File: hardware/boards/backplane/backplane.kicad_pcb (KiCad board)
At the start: 2 copper layers, 47 parts, among them J1 SPARE_I2C, J10 I2C_IN, J11 I2C_OUT, J12 LED_EXT_OUT, J14 DC_IN, J2 SLOT_4, J3 SLOT_1, J4 SLOT_2, J5 SLOT_5, J6 SLOT_6, J7 SLOT_3, J8 LED_EXT_IN, U1 TCA9548APWR, U2 USBLC6-2SC6, U3 USBLC6-2SC6, U4 USBLC6-2SC6, U5 USBLC6-2SC6, U6 USBLC6-2SC6, U7 USBLC6-2SC6

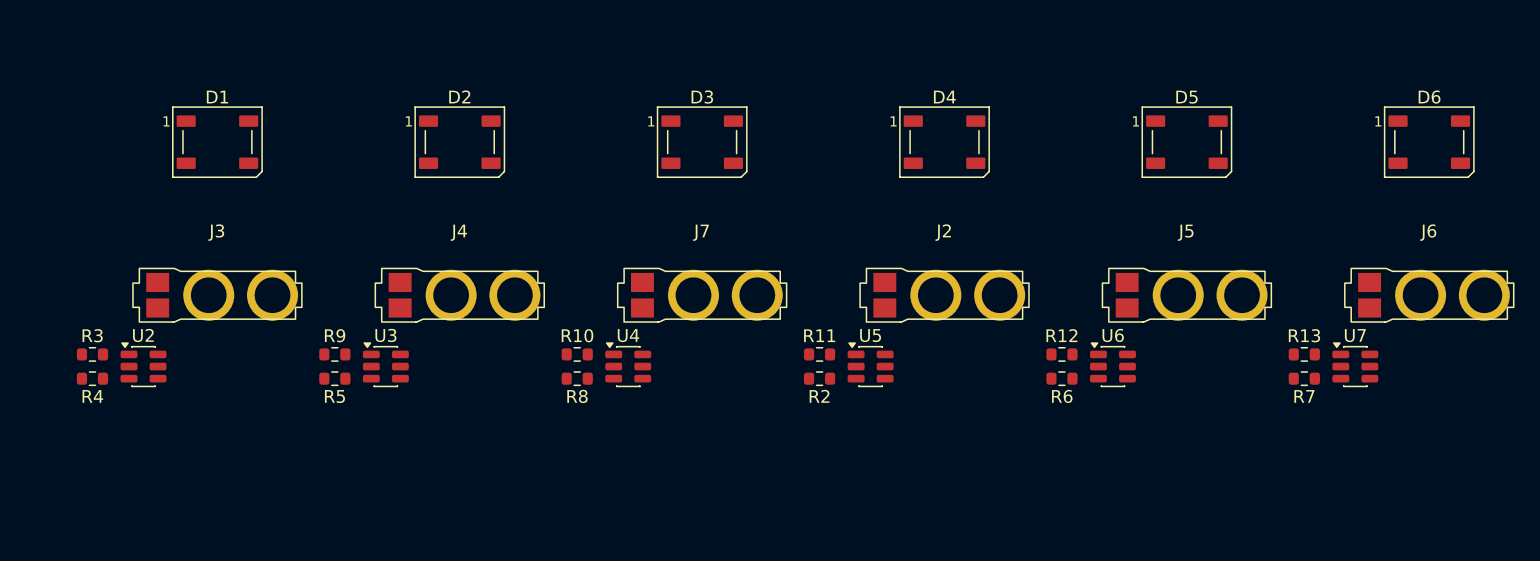
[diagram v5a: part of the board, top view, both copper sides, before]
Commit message: Reorient backplane slot component groups
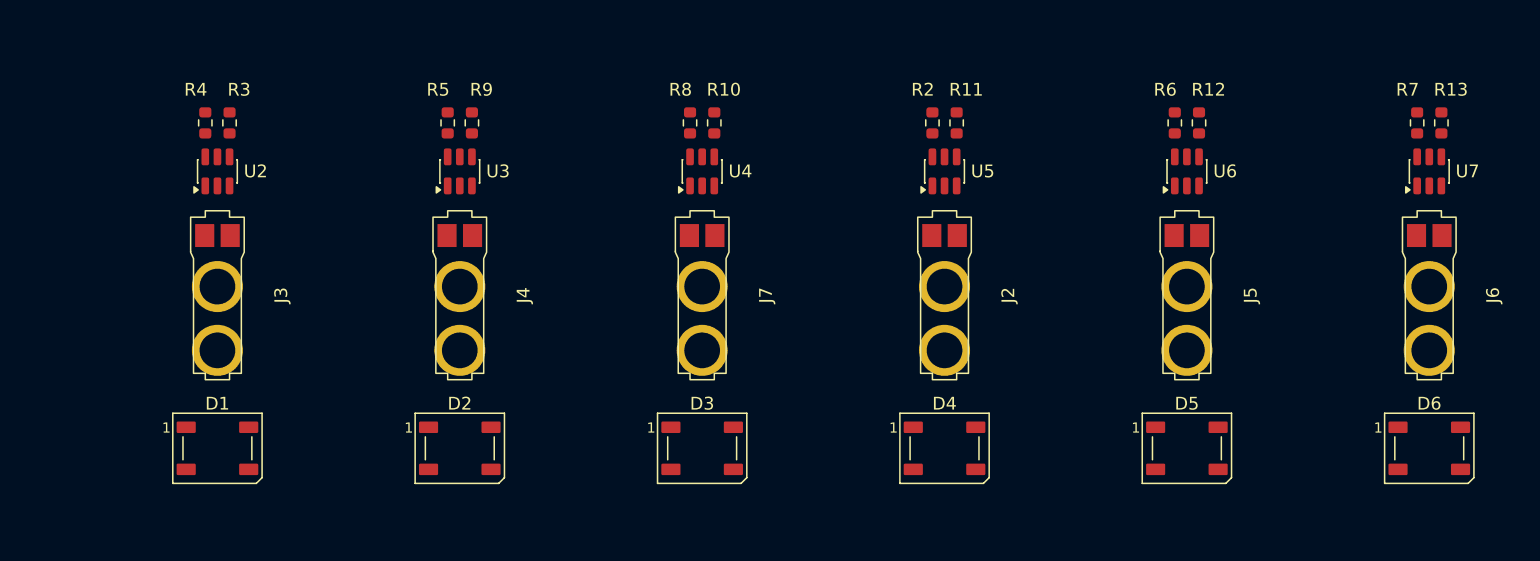
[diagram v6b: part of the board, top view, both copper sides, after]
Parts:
- moved D1 24.0 mm to (68.8, 76.9)
- moved D2 24.0 mm to (87.8, 76.9)
- moved D3 24.0 mm to (106.8, 76.9)
- moved D4 24.0 mm to (125.8, 76.9)
- moved D5 24.0 mm to (144.8, 76.9)
- moved D6 24.0 mm to (163.8, 76.9)
- moved R2 21.9 mm to (124.8, 51.4), turned to 90 degrees
- moved R4 21.9 mm to (67.8, 51.4), turned to 90 degrees
- moved R5 21.9 mm to (86.8, 51.4), turned to 90 degrees
- moved R6 21.9 mm to (143.8, 51.4), turned to 90 degrees
- moved R7 21.9 mm to (162.8, 51.4), turned to 90 degrees
- moved R8 21.9 mm to (105.8, 51.4), turned to 90 degrees
- moved R10 21.1 mm to (107.7, 51.4), turned to 90 degrees
- moved R11 21.1 mm to (126.7, 51.4), turned to 90 degrees
- moved R12 21.1 mm to (145.7, 51.4), turned to 90 degrees
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
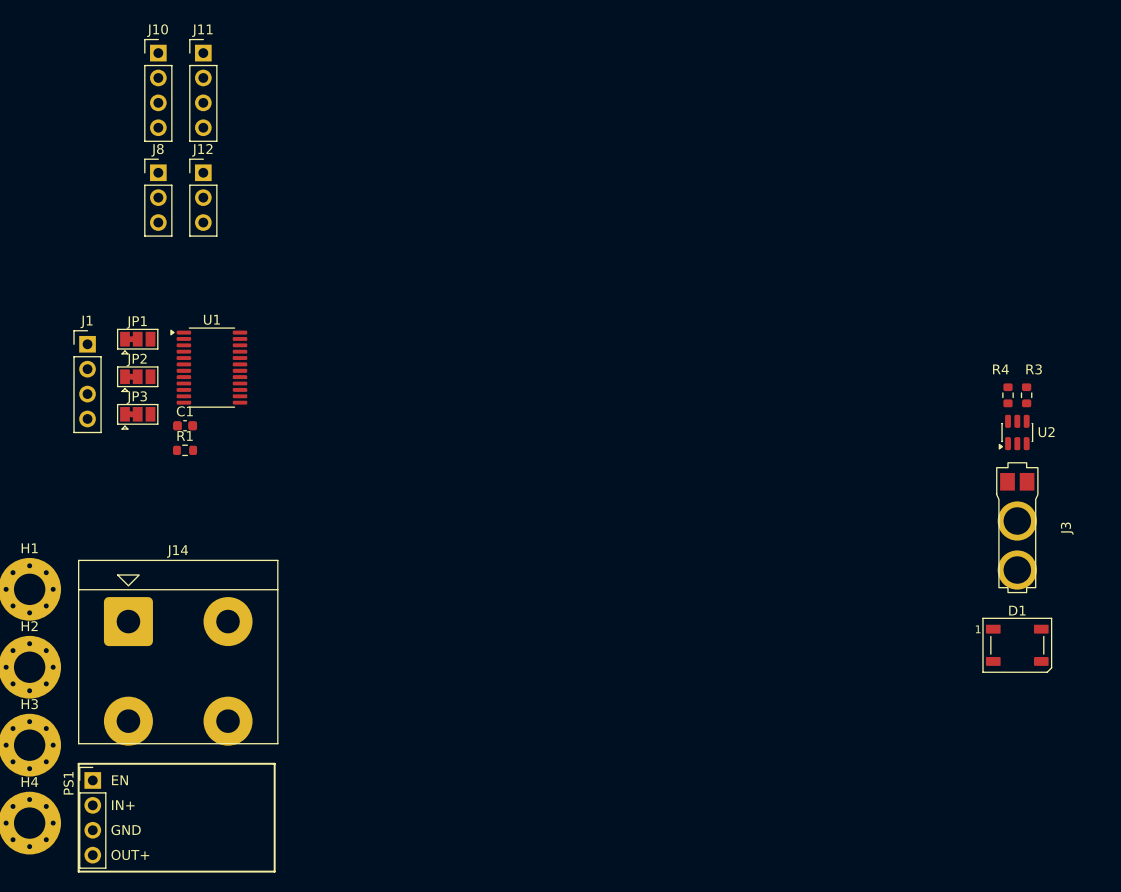
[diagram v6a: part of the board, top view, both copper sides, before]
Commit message: Save initial backplane routing orientations
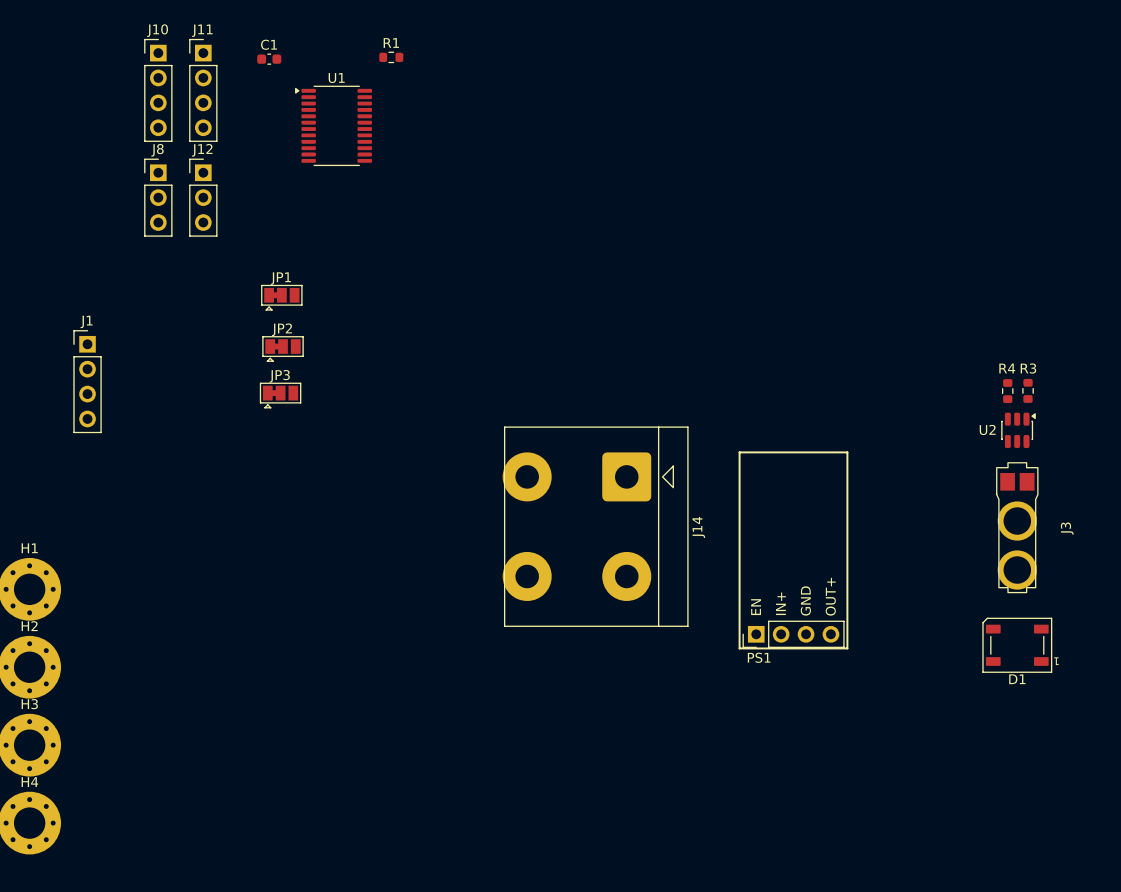
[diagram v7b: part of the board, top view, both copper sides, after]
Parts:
- moved PS1 69.3 mm to (42.2, 75.8), turned to 90 degrees
- moved J14 52.9 mm to (28.9, 59.7), turned to -90 degrees
- moved R1 45.3 mm to (4.92, 16.9)
- moved C1 38.4 mm to (-7.53, 17.1)
- moved U1 27.8 mm to (-0.64, 23.9)
- moved JP1 15.4 mm to (-6.24, 41.2)
- moved JP2 15.1 mm to (-6.12, 46.4)
- moved JP3 14.7 mm to (-6.37, 51.2)
- moved R3 0.47 mm to (69.9, 51.0), turned to -90 degrees
- moved R4 0.43 mm to (67.8, 51.0), turned to -90 degrees
- moved U2 0.22 mm to (68.8, 55.0), turned to -90 degrees
- turned D1 to 180 degrees

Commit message: Repeat slot routing orientations
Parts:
- moved R10 0.47 mm to (107.9, 51.0), turned to -90 degrees
- moved R11 0.47 mm to (126.9, 51.0), turned to -90 degrees
- moved R9 0.47 mm to (88.9, 51.0), turned to -90 degrees
- moved R12 0.47 mm to (145.9, 51.0), turned to -90 degrees
- moved R13 0.47 mm to (164.9, 51.0), turned to -90 degrees
- moved R2 0.43 mm to (124.8, 51.0), turned to -90 degrees
- moved R5 0.43 mm to (86.8, 51.0), turned to -90 degrees
- moved R6 0.43 mm to (143.8, 51.0), turned to -90 degrees
- moved R7 0.43 mm to (162.8, 51.0), turned to -90 degrees
- moved R8 0.43 mm to (105.8, 51.0), turned to -90 degrees
- moved U3 0.22 mm to (87.8, 55.0), turned to -90 degrees
- moved U4 0.22 mm to (106.8, 55.0), turned to -90 degrees
- moved U5 0.22 mm to (125.8, 55.0), turned to -90 degrees
- moved U6 0.22 mm to (144.8, 55.0), turned to -90 degrees
- moved U7 0.22 mm to (163.8, 55.0), turned to -90 degrees
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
